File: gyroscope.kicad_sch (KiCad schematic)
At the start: 1 part, among them U3 IAM-20380

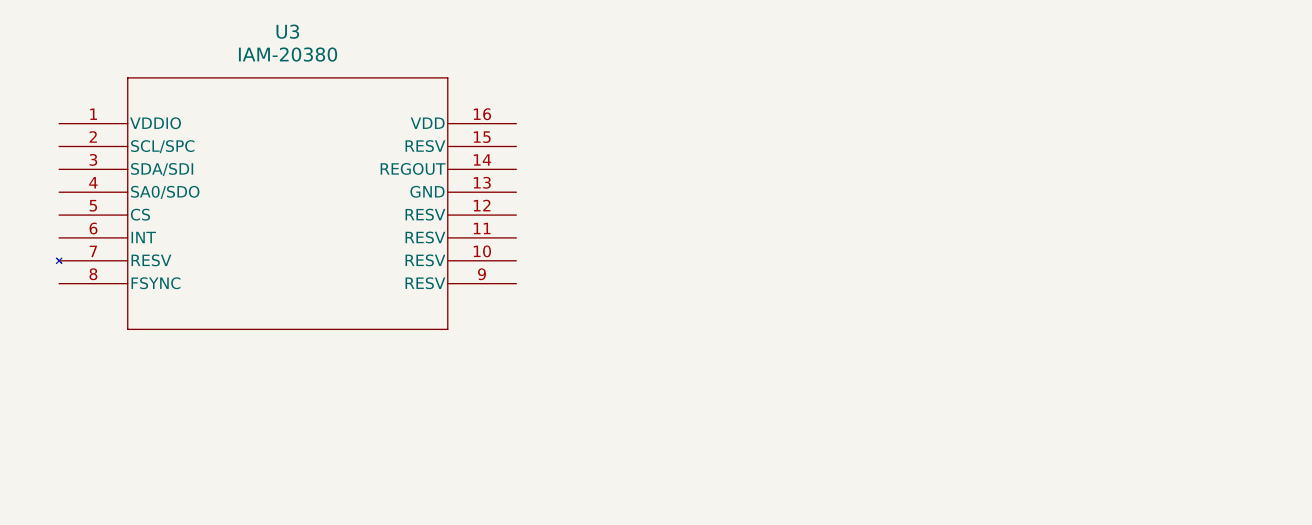
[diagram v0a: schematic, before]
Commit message: added circuitry for magnetometer, gyroscope and h-bridges
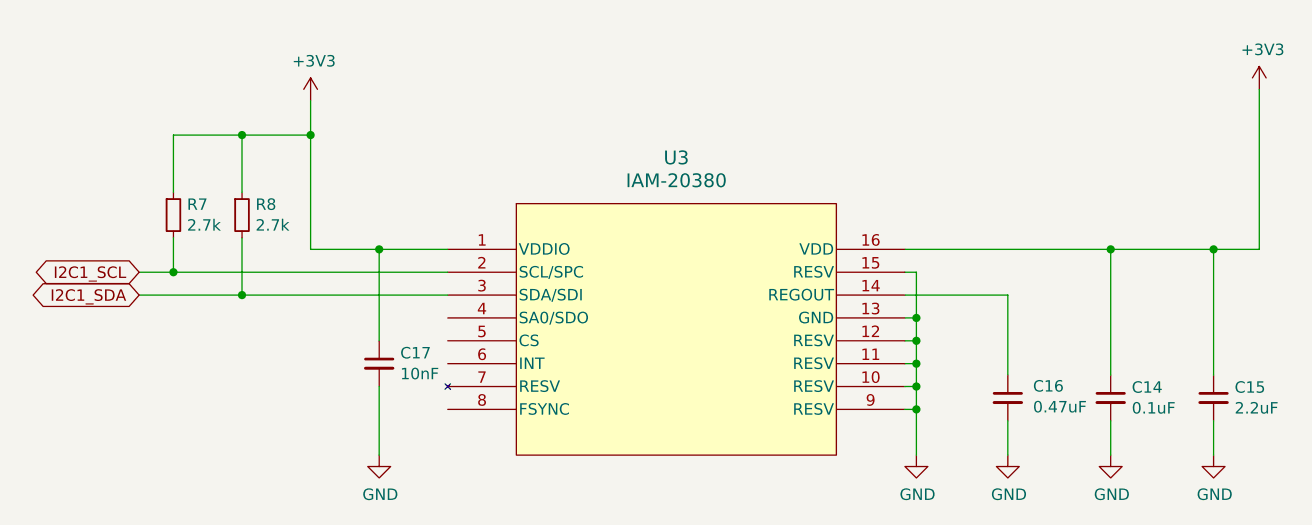
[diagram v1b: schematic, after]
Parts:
- added C14: 0.1uF, Capacitor_SMD:C_0805_2012Metric_Pad1.15x1.40mm_HandSolder, symbol Device:C_Small
- added C15: 2.2uF, Capacitor_SMD:C_0805_2012Metric_Pad1.15x1.40mm_HandSolder, symbol Device:C_Small
- added C16: 0.47uF, Capacitor_SMD:C_0805_2012Metric_Pad1.15x1.40mm_HandSolder, symbol Device:C_Small
- added C17: 10nF, Capacitor_SMD:C_0805_2012Metric_Pad1.15x1.40mm_HandSolder, symbol Device:C_Small
- added R7, R8: 2.7k, Resistor_SMD:R_0805_2012Metric_Pad1.15x1.40mm_HandSolder, symbol Device:R_Small
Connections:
- net +3V3: now reaches U3.1 (VDDIO)
- net +3V3: now also U3.16 (VDD), C14.1, C15.1, C17.1, R7.1, R8.1
- net GND: now reaches U3.10 (RESV)
- net GND: now also U3.11 (RESV), U3.12 (RESV), U3.13 (GND), U3.15 (RESV), U3.9 (RESV), C14.2, C15.2, C16.2, C17.2
- net at U3.14 (REGOUT): now also C16.1
- net I2C1_SCL: now reaches U3.2 (SCL/SPC)
- net I2C1_SCL: now also R7.2
- net I2C1_SDA: now reaches U3.3 (SDA/SDI)
- net I2C1_SDA: now also R8.2
